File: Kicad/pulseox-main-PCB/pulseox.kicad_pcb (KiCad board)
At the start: 2 copper layers, 47.4 x 44.4 mm, 36 parts, among them CON1_MICROUSB1 USB_OTG, CON2 TerminalBlock3.5mm, J1 Jumper_NO_Small, J2 Jumper_NO_Small, J3 CON3, P1 Header 4, P2 Header8, SW1 OS102011MA1QS1, SW2 SW_Push, SW4 SW_Push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

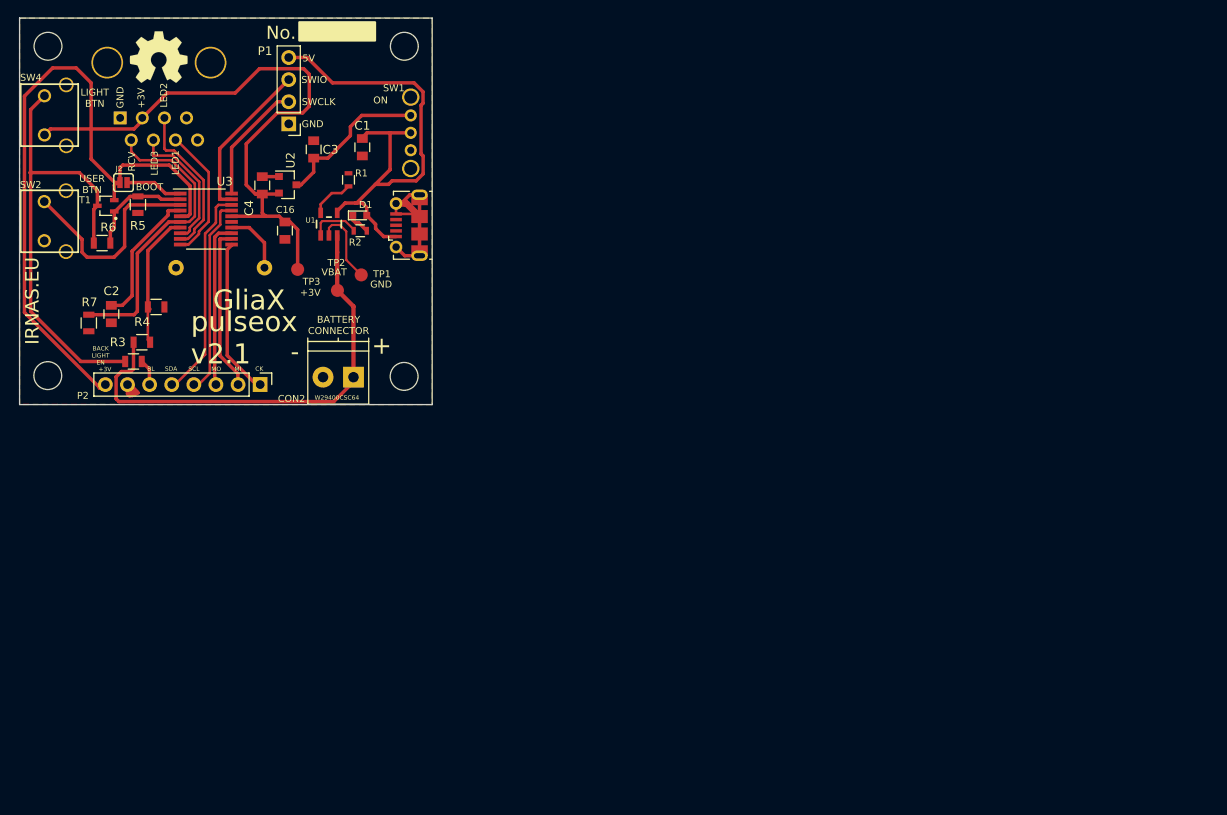
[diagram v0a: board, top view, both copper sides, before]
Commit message: Added output PDF files from Kicad project
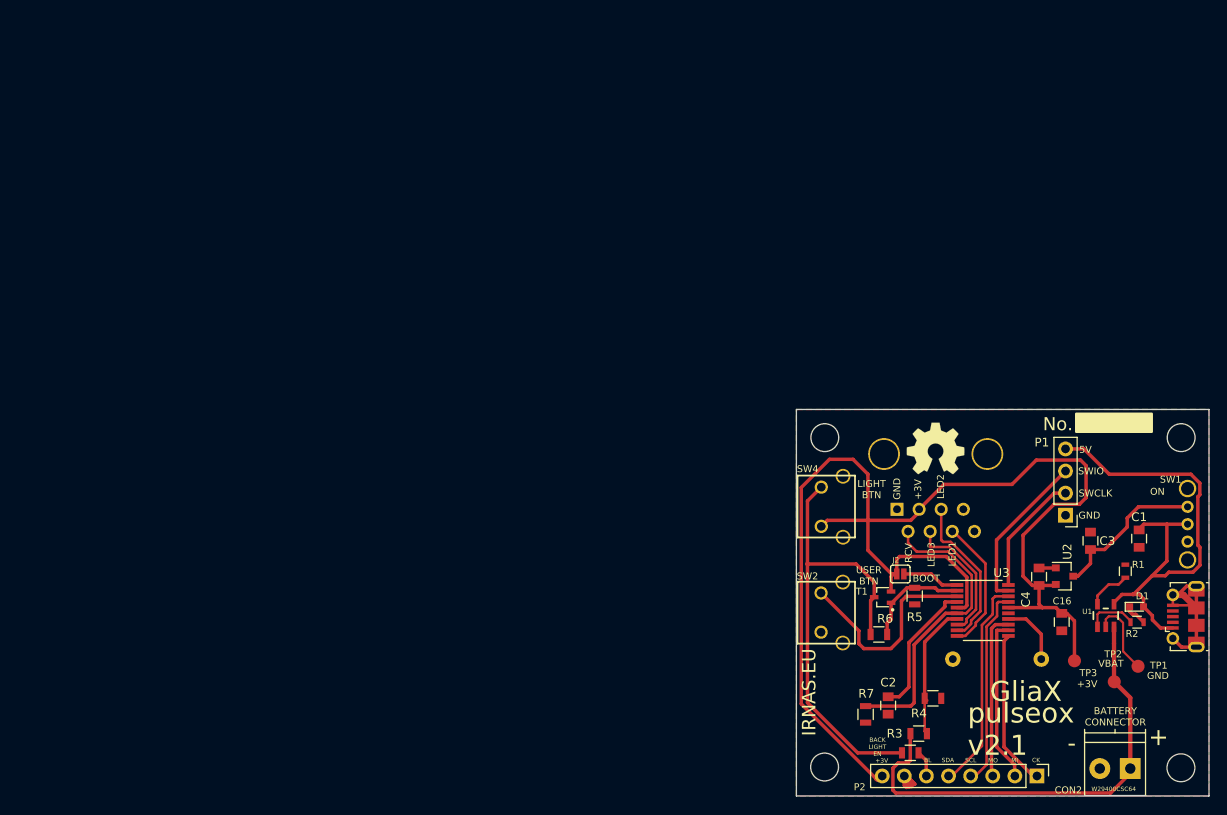
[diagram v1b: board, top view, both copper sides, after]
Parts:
- moved C16 99.9 mm to (147.7, 93.4)
- moved CON2 99.9 mm to (155.5, 110.2)
- moved D1 99.9 mm to (156.2, 91.7)
- moved J2 99.9 mm to (129.1, 87.9)
- moved J3 99.9 mm to (128.7, 80.5)
- moved R2 99.9 mm to (156.3, 93.4)
- moved REF*** 99.9 mm to (133.1, 73.5)
- moved TP3 99.9 mm to (149.1, 97.9)
- moved U2 99.9 mm to (148.0, 88.1)
- moved BUZ1 99.9 mm to (140.2, 97.7)
- moved C1 99.9 mm to (156.5, 83.8)
- moved C2 99.9 mm to (127.7, 103.0)
- moved C3 99.9 mm to (151.0, 84.1)
- moved C4 99.9 mm to (145.0, 88.2)
- moved CON1_MICROUSB1 99.9 mm to (162.8, 92.8)
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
